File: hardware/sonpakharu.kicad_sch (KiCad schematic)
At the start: 1 part, among them IC1 ESP32-S3-WROOM-1U-N4

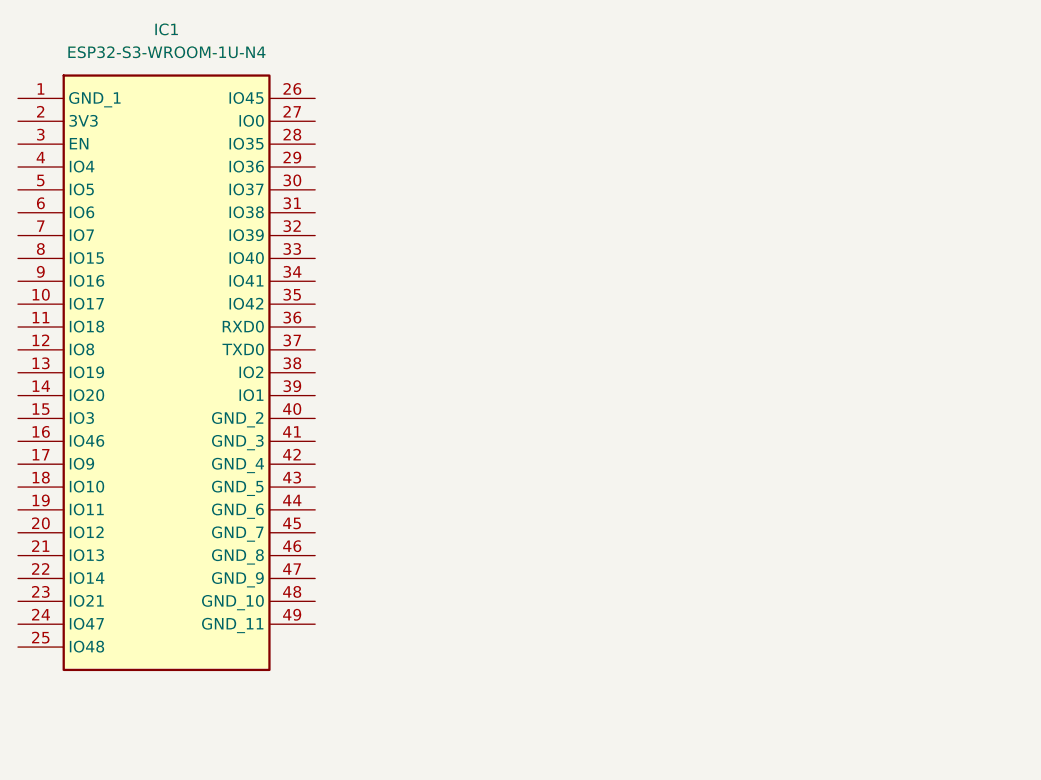
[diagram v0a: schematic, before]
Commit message: added usb otg
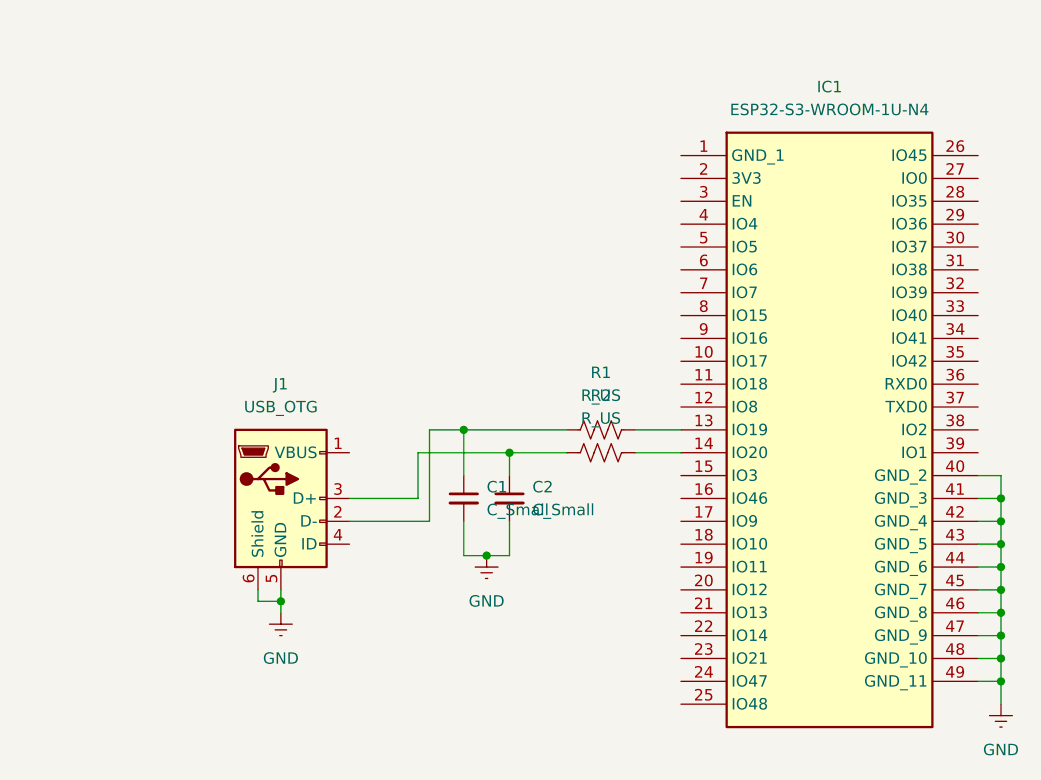
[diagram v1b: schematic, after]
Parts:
- added C1, C2: C_Small, symbol Device:C_Small
- added J1: USB_OTG, symbol Connector:USB_OTG
- added R1, R2: R_US, symbol Device:R_US
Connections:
- net at IC1.13 (IO19): now also R1.1
- net at IC1.14 (IO20): now also R2.1
- net GND: now reaches IC1.40 (GND_2)
- net GND: now also IC1.41 (GND_3), IC1.42 (GND_4), IC1.43 (GND_5), IC1.44 (GND_6), IC1.45 (GND_7), IC1.46 (GND_8), IC1.47 (GND_9), IC1.48 (GND_10), IC1.49 (GND_11), C1.2, C2.2, J1.5 (GND), J1.6 (Shield)
- new net: C1.1, J1.2 (D-), R1.2
- new net: C2.1, J1.3 (D+), R2.2
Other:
- moved on the sheet: IC1

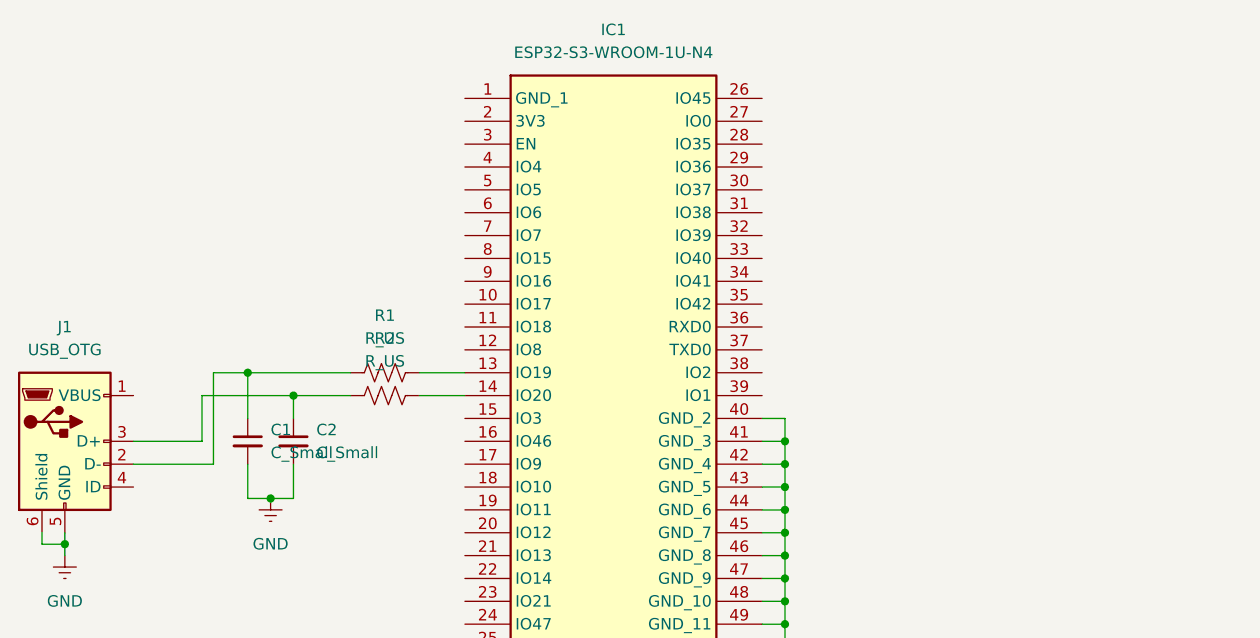
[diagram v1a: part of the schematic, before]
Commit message: added uart,reset
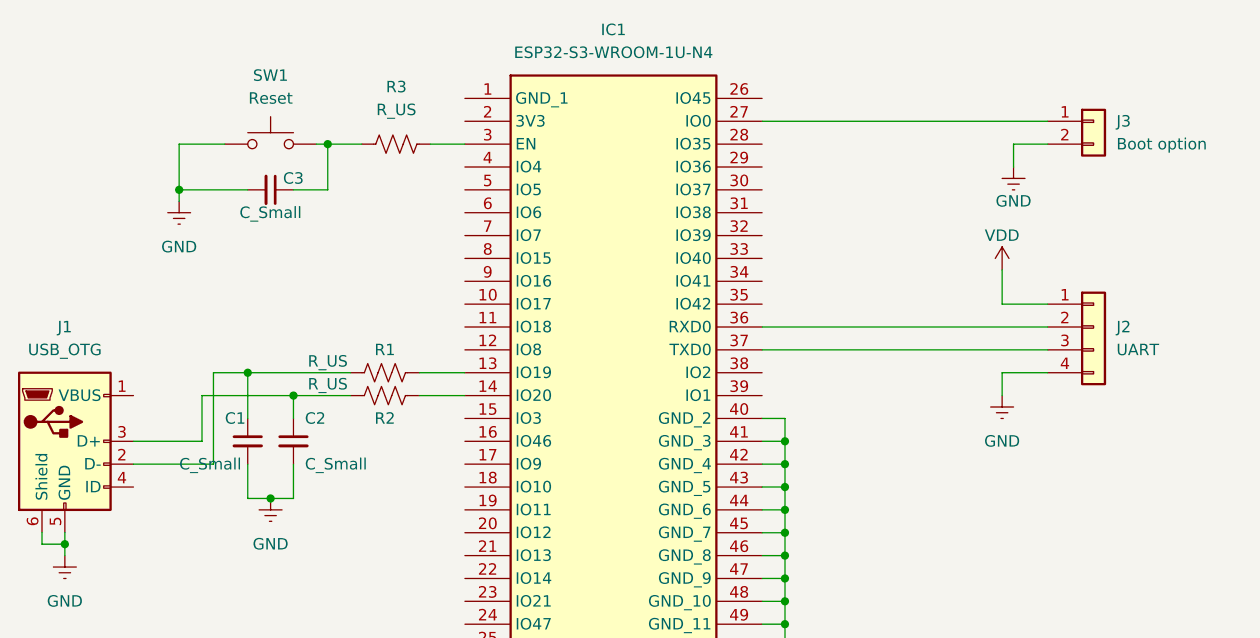
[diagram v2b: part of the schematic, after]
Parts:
- added C3: C_Small, symbol Device:C_Small
- added J2: UART, symbol Connector_Generic:Conn_01x04
- added J3: Boot option, symbol Connector_Generic:Conn_01x02
- added R3: R_US, symbol Device:R_US
- added SW1: Reset, symbol Switch:SW_Push
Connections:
- net GND: now also C3.2, J2.4 (Pin_4), J3.2 (Pin_2), SW1.1
- net at IC1.27 (IO0): now also J3.1 (Pin_1)
- net at IC1.3 (EN): now also R3.1
- net at IC1.36 (RXD0): now also J2.2 (Pin_2)
- net at IC1.37 (TXD0): now also J2.3 (Pin_3)
- new net: C3.1, R3.2, SW1.2
- new net VDD: J2.1 (Pin_1)

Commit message: minor changes
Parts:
- added C4: 22uF, symbol Device:C_Small
- added C5: 0.1uF, symbol Device:C_Small
- added C6: C_Small, symbol Device:C_Small
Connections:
- net GND: now also C4.2, C5.2, C6.1
- net at IC1.1 (GND_1): now also C6.2
- net +3V3: now reaches IC1.2 (3V3)
- net +3V3: now also C4.1, C5.1
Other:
- moved on the sheet: C3, R3, SW1

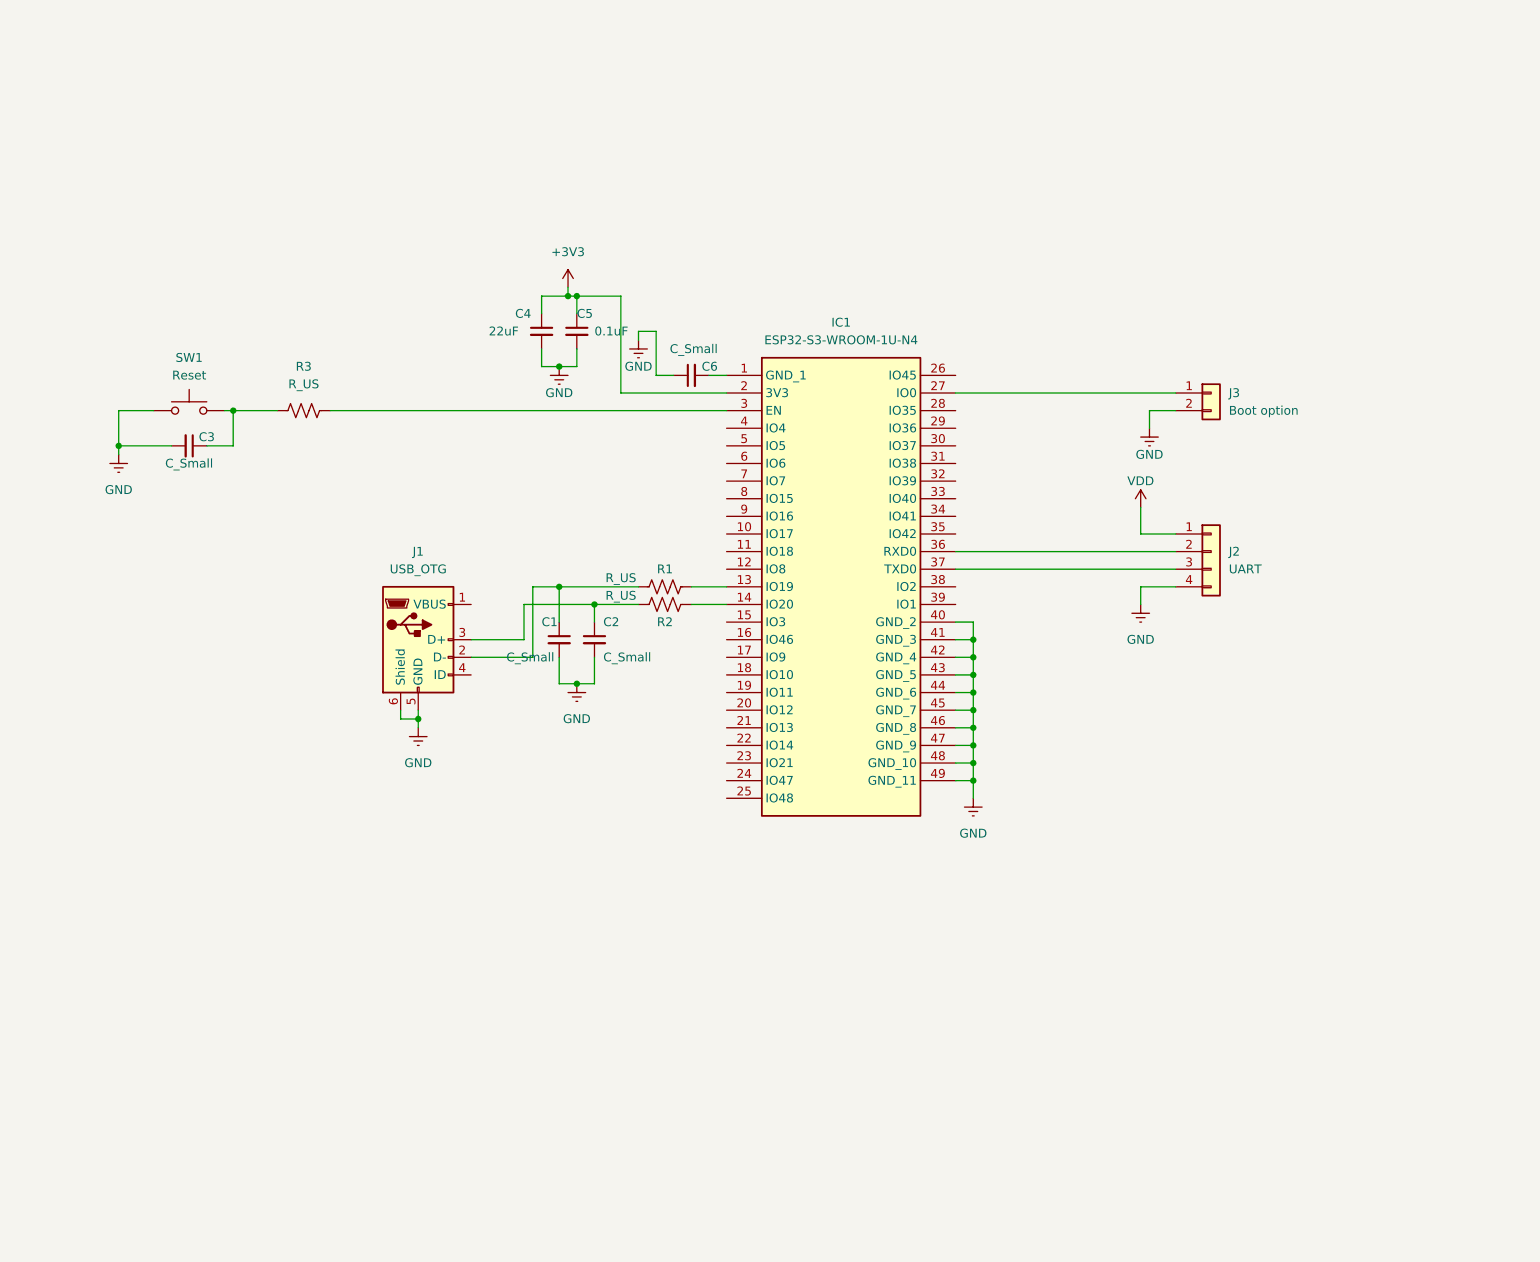
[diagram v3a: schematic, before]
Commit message: added power and program ckt
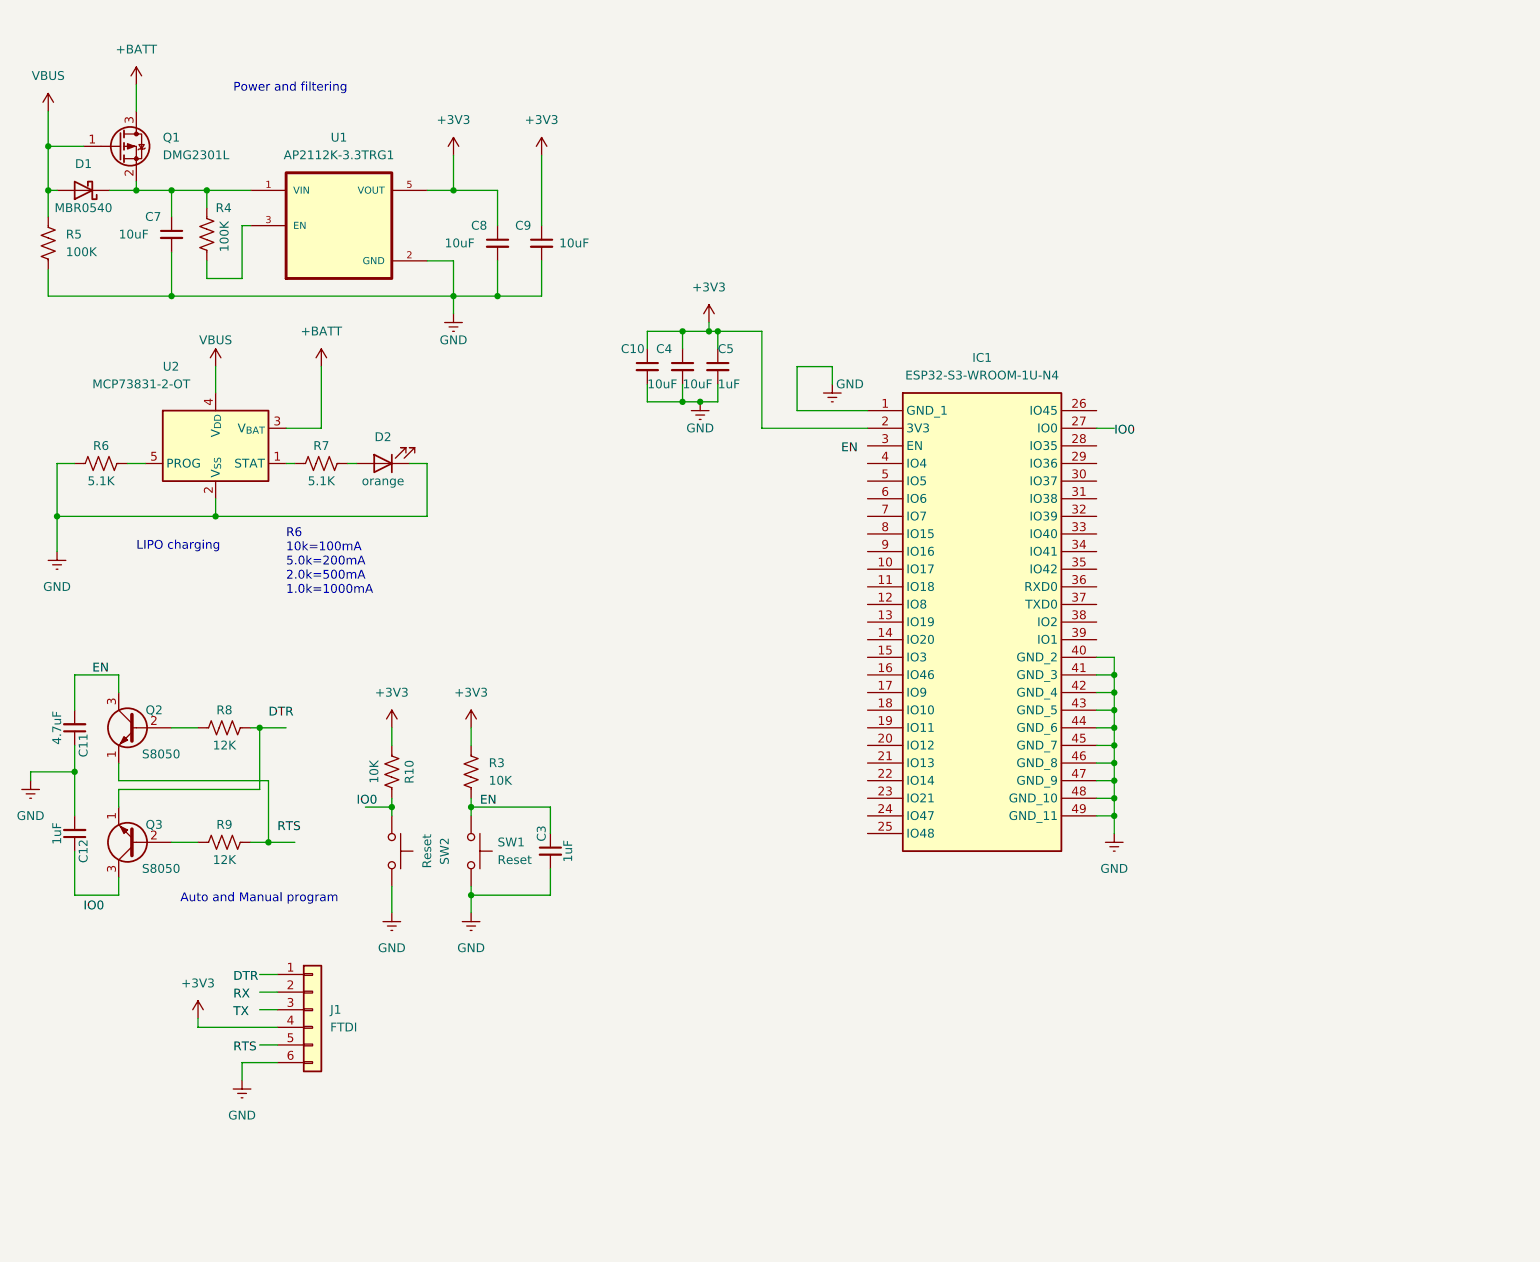
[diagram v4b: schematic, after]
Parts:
- removed C1, C2, C6: C_Small, symbol Device:C_Small
- removed J1: USB_OTG, symbol Connector:USB_OTG
- removed J2: UART, symbol Connector_Generic:Conn_01x04
- removed J3: Boot option, symbol Connector_Generic:Conn_01x02
- removed R1, R2: R_US, symbol Device:R_US
- added C10, C7, C8, C9: 10uF, symbol Device:C_Small
- added C11: 4.7uF, symbol Device:C_Small
- added C12: 1uF, symbol Device:C_Small
- added D1: MBR0540, Diode_SMD:D_SOD-123, symbol Diode:MBR0540
- added D2: orange, symbol Device:LED
- added J1: FTDI, symbol Connector_Generic:Conn_01x06
- added Q1: DMG2301L, Package_TO_SOT_SMD:SOT-23, symbol Transistor_FET:DMG2301L
- added Q2, Q3: S8050, Package_TO_SOT_THT:TO-92_Inline, symbol Transistor_BJT:S8050
- added R10: 10K, symbol Device:R_US
- added R4, R5: 100K, symbol Device:R_US
- added R6, R7: 5.1K, symbol Device:R_US
- added R8, R9: 12K, symbol Device:R_US
- added SW2: Reset, symbol Switch:SW_Push
- added U1: AP2112K-3.3TRG1, AP2112K-3.3TRG1:SOT95P285X140-5N, symbol AP2112K-3.3TRG1:AP2112K-3.3TRG1
- added U2: MCP73831-2-OT, Package_TO_SOT_SMD:SOT-23-5, symbol Battery_Management:MCP73831-2-OT
- C3: value C_Small -> 1uF
- C4: value 22uF -> 10uF
- C5: value 0.1uF -> 1uF
- R3: value R_US -> 10K
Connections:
- net +3V3: now also R3.2, C10.1, C8.1, C9.1, J1.4 (Pin_4), R10.1, U1.5 (VOUT)
- net GND: now also IC1.1 (GND_1), SW1.2, C10.2, C11.1, C12.2, C7.2, C8.2, C9.2, D2.1 (K), J1.6 (Pin_6), R5.1, R6.1, SW2.2, U1.2 (GND), U2.2 (V_{SS}); no longer SW1.1
- net at IC1.3 (EN): no longer R3.1
- new net: R10.2, SW2.1
- new net: C12.1, Q3.3 (C)
- new net: Q2.2 (B), R8.1
- new net: Q3.1 (E), R8.2
- new net: Q3.2 (B), R9.1
- new net: R7.1, U2.1 (STAT)
- new net: R6.2, U2.5 (PROG)
- new net: R4.1, U1.3 (EN)
- new net: C7.1, D1.1 (K), Q1.2 (S), R4.2, U1.1 (VIN)
- new net: D2.2 (A), R7.2
- new net: Q2.1 (E), R9.2
- new net +BATT: Q1.3 (D), U2.3 (V_{BAT})
- new net EN: C11.2, C3.1, Q2.3 (C), R3.1, SW1.1
- new net VBUS: D1.2 (A), Q1.1 (G), R5.2, U2.4 (V_{DD})
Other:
- note added: "Auto and Manual program"
- note added: "LIPO charging"
- note added: "Power and filtering"
- note added: "R6 10k=100mA 5.0k=200mA 2.0k=500mA 1.0k=1000mA"
- moved on the sheet: C3, C4, C5, IC1, R3, SW1
